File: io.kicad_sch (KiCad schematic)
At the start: 20 parts, among them J1 USB_C_Receptacle_USB2.0_14P, J2 Micro_SD_Card, U3 FT2232HL, Y1 12Mhz

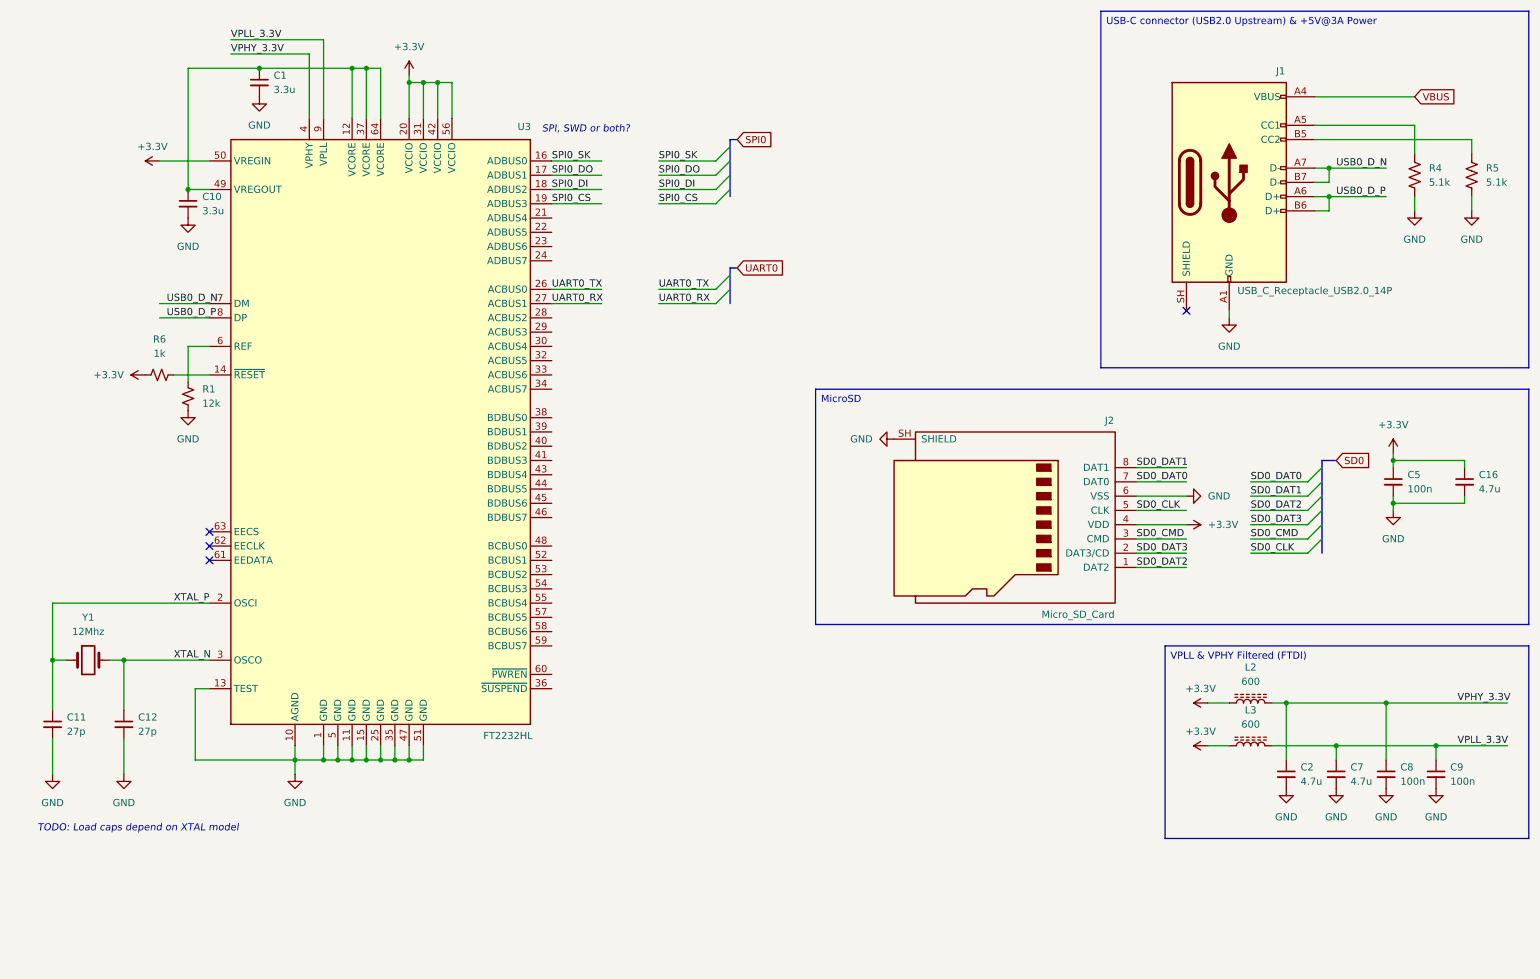
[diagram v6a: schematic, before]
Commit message: A lot re-wiring, added appropriate parts for schematic components. Some re-organization.
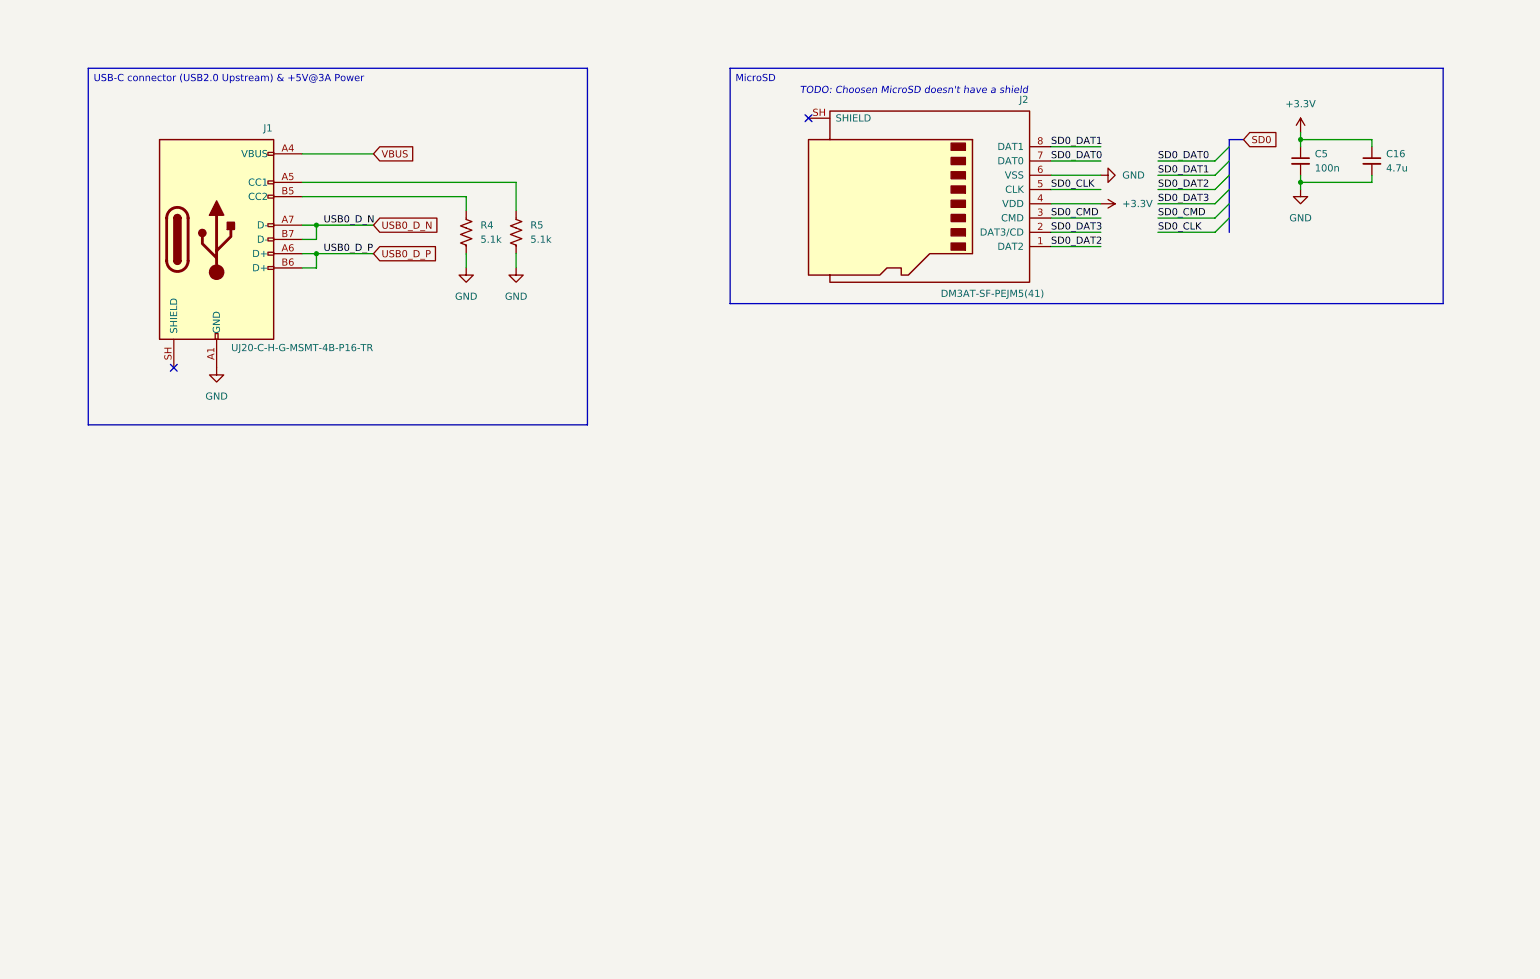
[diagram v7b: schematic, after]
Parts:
- removed C1, C10: 3.3u, symbol Device:C_Small
- removed C11, C12: 27p, symbol Device:C_Small
- removed C2, C7: 4.7u, symbol Device:C_Small
- removed C8, C9: 100n, symbol Device:C_Small
- removed L2, L3: 600, symbol Device:L_Ferrite
- removed R1: 12k, symbol Device:R_Small_US
- removed R6: 1k, symbol Device:R_Small_US
- removed U3: FT2232HL, Package_QFP:LQFP-64_10x10mm_P0.5mm, symbol Interface_USB:FT2232HL
- removed Y1: 12Mhz, symbol Device:Crystal
- J1: value USB_C_Receptacle_USB2.0_14P -> UJ20-C-H-G-MSMT-4B-P16-TR
- J2: value Micro_SD_Card -> DM3AT-SF-PEJM5(41)
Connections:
- net GND: no longer J2.SH (SHIELD)
- net at R4.1: now also J1.B5 (CC2); no longer J1.A5 (CC1)
- net at R5.1: now also J1.A5 (CC1); no longer J1.B5 (CC2)
- no-connect marks 4 -> 2
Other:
- note added: "TODO: Choosen MicroSD doesn't have a shield"
- note removed: "SPI, SWD or both?"
- note removed: "TODO: Load caps depend on XTAL model"
- moved on the sheet: C16, C5, J1, J2, R4, R5

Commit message: Alot of stuff
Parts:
- removed J1: UJ20-C-H-G-MSMT-4B-P16-TR, symbol Connector:USB_C_Receptacle_USB2.0_14P
- removed J2: DM3AT-SF-PEJM5(41), symbol Connector:Micro_SD_Card
- added J1: USB_C_Receptacle_USB2.0_16P, SamacSys_Parts:UJ20CHGMSMT4BP16TR, symbol advres:USB_C_Receptacle_USB2.0_16P
- added J3: Micro_SD_Card_Det_Hirose_DM3AT, SamacSys_Parts:DM3ATSFPEJM541, symbol advres:Micro_SD_Card_Det_Hirose_DM3AT
- added R1, R21, R24, R6: 10k, symbol Device:R_US
- added S1: DS04-254-1S-05BK, SamacSys_Parts:DS04-254-1S-05BK, symbol advres:SW_DIP_x05
- added S2: TS02-66-50-BK-100-LCR-D, TS0266100BK100LCRD, symbol SamacSys_Parts:TS02-66-50-BK-100-LCR-D
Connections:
- net +3.3V: now also J3.4 (VDD), J3.MP3 (DET_A), S1.6, S1.7, S1.8
- net GND: now also J1.A1 (GND), J1.A12 (GND), J1.B1 (GND), J1.B12 (GND), J3.6 (VSS), R1.2, R21.2, R24.2, R6.2, S2.1 (NO_1), S2.2 (NO_2)
- net SD0_CLK: now also J3.5 (CLK)
- net SD0_CMD: now also J3.3 (CMD)
- net SD0_DAT0: now also J3.7 (DAT0)
- net SD0_DAT1: now also J3.8 (DAT1)
- net SD0_DAT2: now also J3.1 (DAT2)
- net SD0_DAT3: now also J3.2 (DAT3/CD)
- net USB0_D_N: now also J1.A7 (D-), J1.B7 (D-)
- net USB0_D_P: now also J1.A6 (D+), J1.B6 (D+)
- net VBUS: now also J1.A4 (VBUS), J1.A9 (VBUS), J1.B4 (VBUS), J1.B9 (VBUS)
- net at R4.1: now also J1.B5 (CC2)
- net at R5.1: now also J1.A5 (CC1)
- new net: J1.MH1 (MH), J1.MH2, J1.MH3, J1.MH4
- new net: J3.MP1 (MP), J3.MP2 (MP), J3.MP4 (MP), J3.MP5 (MP), J3.MP6 (MP)
- new net JT_I2C_SW: R24.1, S1.3
- new net MCU_BOOT0: R6.1, S1.1
- new net MCU_BOOT1: R21.1, S1.2
- new net MCU_NRST: S2.4 (COM_2)
- new net SD0_DET: J3.MP7 (DET_B), R1.1
- no-connect marks 2 -> 9
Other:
- note added: "JT_I2C_SW LOW: I2C HI: JTAG via FTDI"
- note added: "MCU Reset switch"
- note added: "MCU_BOOTx 0x: Main Flash 10: System Memory, STM Bootloader 11: Embedded SRAM"
- note removed: "TODO: Choosen MicroSD doesn't have a shield"
- moved on the sheet: C16, C5
